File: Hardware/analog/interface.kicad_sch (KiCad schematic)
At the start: 21 parts, among them J301 Conn_02x10_Odd_Even, U301 ADUM131D, U302 ADUM131D, U303 ADUM1250, U304 74LVC1G19

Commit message: More tweaks to load board
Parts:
- added C312: 100nF, Capacitor_SMD:C_0805_2012Metric_Pad1.18x1.45mm_HandSolder, symbol Device:C_Small
- added JP301: Cfg WP, Connector_PinHeader_2.54mm:PinHeader_1x03_P2.54mm_Vertical, symbol Jumper:SolderJumper_3_Bridged12
- added U305: AT24CS32-SSHM, Package_SO:SOIC-8_3.9x4.9mm_P1.27mm, symbol Memory_EEPROM:AT24CS32-SSHM
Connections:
- net +3V3: now also C312.1, JP301.3 (B), U305.8 (VCC)
- net GND: now also C312.2, JP301.1 (A), U305.1 (A0), U305.2 (A1), U305.3 (A2), U305.4 (GND)
- net I2C_SCL: now also U305.6 (SCL)
- net I2C_SDA: now also U305.5 (SDA)
- new net: JP301.2 (C), U305.7 (WP)
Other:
- note added: "IDPROM"
- note added: "I²C address: 0b1010000/0b1011000"

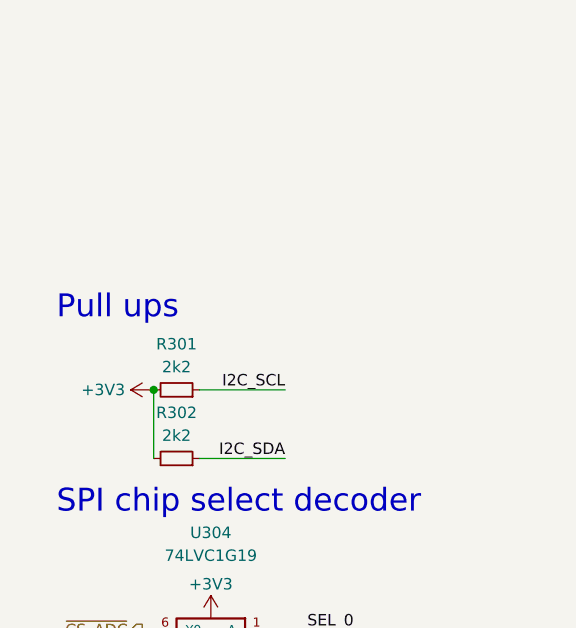
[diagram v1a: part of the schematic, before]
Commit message: Added ADC/DAC section
- Imported the schematic for the analog DAC/ADC section, as well as the
  Vref generator and clock generator for the ADC
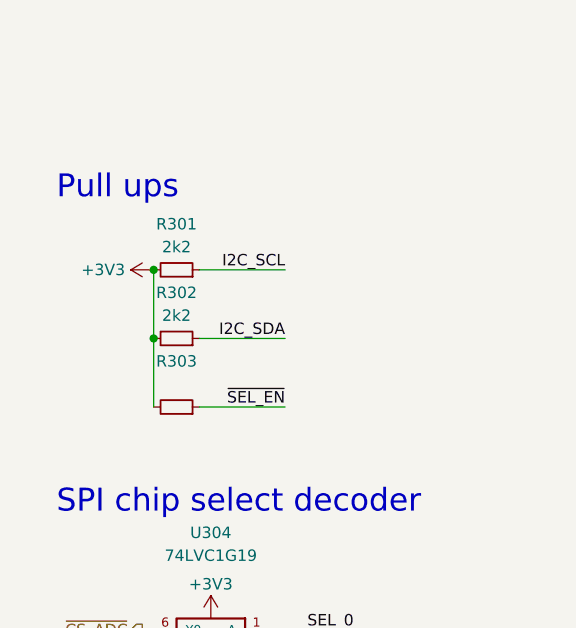
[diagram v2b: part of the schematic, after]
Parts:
- added R303: (no value), symbol Device:R_Small
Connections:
- net +3V3: now also R303.2
- net ~{SEL_EN}: now also R303.1
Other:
- moved on the sheet: R301, R302
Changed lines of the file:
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@@
   (junction (at 175.26 25.4) (diameter 0) (color 0 0 0 0)
   )
+  (junction (at 25.4 151.765) (diameter 0) (color 0 0 0 0)
+  )
   (junction (at 144.78 25.4) (diameter 0) (color 0 0 0 0)
   )
@@
   (junction (at 136.525 30.48) (diameter 0) (color 0 0 0 0)
   )
-  (junction (at 25.4 157.48) (diameter 0) (color 0 0 0 0)
+  (junction (at 25.4 144.145) (diameter 0) (color 0 0 0 0)
   )
   (junction (at 273.05 150.495) (diameter 0) (color 0 0 0 0)
@@
     (stroke (width 0) (type default) (color 0 0 0 0))
   )
-  (wire (pts (xy 40.005 157.48) (xy 30.48 157.48))
+  (wire (pts (xy 40.005 144.145) (xy 30.48 144.145))
     (stroke (width 0) (type default) (color 0 0 0 0))
   )
@@
     (stroke (width 0) (type default) (color 0 0 0 0))
   )
+  (wire (pts (xy 40.005 159.385) (xy 30.48 159.385))
+    (stroke (width 0) (type default) (color 0 0 0 0))
+  )
+  (wire (pts (xy 25.4 151.765) (xy 25.4 159.385))
+    (stroke (width 0) (type default) (color 0 0 0 0))
+  )
   (wire (pts (xy 141.605 80.01) (xy 151.13 80.01))
     (stroke (width 0) (type default) (color 0 0 0 0))
@@
     (stroke (width 0) (type default) (color 0 0 0 0))
   )
-  (wire (pts (xy 40.005 165.1) (xy 30.48 165.1))
+  (wire (pts (xy 40.005 151.765) (xy 30.48 151.765))
     (stroke (width 0) (type default) (color 0 0 0 0))
   )
@@
     (stroke (width 0) (type default) (color 0 0 0 0))
   )
-  (wire (pts (xy 25.4 157.48) (xy 25.4 165.1))
+  (wire (pts (xy 25.4 144.145) (xy 25.4 151.765))
     (stroke (width 0) (type default) (color 0 0 0 0))
   )
@@
     (effects (font (size 1.27 1.27)) (justify left bottom))
   )
-  (text "Pull ups" (at 14.605 149.86 0)
+  (text "Pull ups" (at 14.605 136.525 0)
     (effects (font (size 2.54 2.54)) (justify left bottom))
   )
@@
     (effects (font (size 2.54 2.54)) (justify left bottom))
   )
-  (label "I2C_SDA" (at 40.005 165.1 180)
+  (label "I2C_SDA" (at 40.005 151.765 180)
     (effects (font (size 1.27 1.27)) (justify right bottom))
   )
@@
     (effects (font (size 1.27 1.27)) (justify left bottom))
   )
+  (label "~{SEL_EN}" (at 40.005 159.385 180)
+    (effects (font (size 1.27 1.27)) (justify right bottom))
+  )
   (label "~{IN_SPI_CS}" (at 181.61 77.47 180)
     (effects (font (size 1.27 1.27)) (justify right bottom))
@@
     (effects (font (size 1.27 1.27)) (justify right bottom))
   )
-  (label "I2C_SCL" (at 40.005 157.48 180)
+  (label "I2C_SCL" (at 40.005 144.145 180)
     (effects (font (size 1.27 1.27)) (justify right bottom))
   )
@@
     (pin "1")
   )
-  (symbol (lib_id "Device:R_Small") (at 27.94 165.1 270) (mirror x) (unit 1)
-    (in_bom yes) (on_board yes)
-    (property "Reference" "R302" (id 0) (at 27.94 160.02 90))
-    (property "Value" "2k2" (id 1) (at 27.94 162.56 90))
-    (property "Footprint" "Resistor_SMD:R_0805_2012Metric_Pad1.20x1.40mm_HandSolder" (id 2) (at 27.94 165.1 0)
-      (effects (font (size 1.27 1.27)) hide)
-    )
-    (property "Datasheet" "~" (id 3) (at 27.94 165.1 0)
-      (effects (font (size 1.27 1.27)) hide)
-    )
-    (property "MPN" "RMC1/10-222JTP" (id 4) (at 27.94 165.1 90)
+  (symbol (lib_id "Device:R_Small") (at 27.94 151.765 270) (mirror x) (unit 1)
+    (in_bom yes) (on_board yes)
+    (property "Reference" "R302" (id 0) (at 27.94 146.685 90))
+    (property "Value" "2k2" (id 1) (at 27.94 149.225 90))
+    (property "Footprint" "Resistor_SMD:R_0805_2012Metric_Pad1.20x1.40mm_HandSolder" (id 2) (at 27.94 151.765 0)
+      (effects (font (size 1.27 1.27)) hide)
+    )
+    (property "Datasheet" "~" (id 3) (at 27.94 151.765 0)
+      (effects (font (size 1.27 1.27)) hide)
+    )
+    (property "MPN" "RMC1/10-222JTP" (id 4) (at 27.94 151.765 90)
       (effects (font (size 1.27 1.27)) hide)
     )
@@
     (pin "1")
   )
-  (symbol (lib_id "power:+3V3") (at 25.4 157.48 90) (mirror x) (unit 1)
-    (in_bom yes) (on_board yes) (fields_autoplaced)
-    (property "Reference" "#PWR0331" (id 0) (at 29.21 157.48 0)
-      (effects (font (size 1.27 1.27)) hide)
-    )
-    (property "Value" "+3V3" (id 1) (at 22.225 157.4799 90)
-      (effects (font (size 1.27 1.27)) (justify left))
-    )
-    (property "Footprint" "" (id 2) (at 25.4 157.48 0)
-      (effects (font (size 1.27 1.27)) hide)
-    )
-    (property "Datasheet" "" (id 3) (at 25.4 157.48 0)
+  (symbol (lib_id "power:+3V3") (at 25.4 144.145 90) (mirror x) (unit 1)
+    (in_bom yes) (on_board yes) (fields_autoplaced)
+    (property "Reference" "#PWR0331" (id 0) (at 29.21 144.145 0)
+      (effects (font (size 1.27 1.27)) hide)
+    )
+    (property "Value" "+3V3" (id 1) (at 22.225 144.1449 90)
+      (effects (font (size 1.27 1.27)) (justify left))
+    )
+    (property "Footprint" "" (id 2) (at 25.4 144.145 0)
+      (effects (font (size 1.27 1.27)) hide)
+    )
+    (property "Datasheet" "" (id 3) (at 25.4 144.145 0)
       (effects (font (size 1.27 1.27)) hide)
     )
@@
     )
     (pin "1")
+  )
+  (symbol (lib_id "Device:R_Small") (at 27.94 159.385 270) (mirror x) (unit 1)
+    (in_bom yes) (on_board yes)
+    (property "Reference" "R303" (id 0) (at 27.94 154.305 90))
+    (property "Value" "" (id 1) (at 27.94 156.845 90))
+    (property "Footprint" "" (id 2) (at 27.94 159.385 0)
+      (effects (font (size 1.27 1.27)) hide)
+    )
+    (property "Datasheet" "~" (id 3) (at 27.94 159.385 0)
+      (effects (font (size 1.27 1.27)) hide)
+    )
+    (property "MPN" "RMC1/10-103JTP" (id 4) (at 27.94 159.385 90)
+      (effects (font (size 1.27 1.27)) hide)
+    )
+    (pin "1")
+    (pin "2")
   )
   (symbol (lib_id "power:GND2") (at 190.5 30.48 0) (unit 1)
@@
     (pin "1")
   )
-  (symbol (lib_id "Device:R_Small") (at 27.94 157.48 270) (mirror x) (unit 1)
-    (in_bom yes) (on_board yes)
-    (property "Reference" "R301" (id 0) (at 27.94 152.4 90))
-    (property "Value" "2k2" (id 1) (at 27.94 154.94 90))
-    (property "Footprint" "Resistor_SMD:R_0805_2012Metric_Pad1.20x1.40mm_HandSolder" (id 2) (at 27.94 157.48 0)
-      (effects (font (size 1.27 1.27)) hide)
-    )
-    (property "Datasheet" "~" (id 3) (at 27.94 157.48 0)
-      (effects (font (size 1.27 1.27)) hide)
-    )
-    (property "MPN" "RMC1/10-222JTP" (id 4) (at 27.94 157.48 90)
-      (effects (font (size 1.27 1.27)) hide)
-    )
+  (symbol (lib_id "Device:R_Small") (at 27.94 144.145 270) (mirror x) (unit 1)
+    (in_bom yes) (on_board yes)
+    (property "Reference" "R301" (id 0) (at 27.94 139.065 90))
+    (property "Value" "2k2" (id 1) (at 27.94 141.605 90))
+    (property "Footprint" "Resistor_SMD:R_0805_2012Metric_Pad1.20x1.40mm_HandSolder" (id 2) (at 27.94 144.145 0)
+      (effects (font (size 1.27 1.27)) hide)
+    )
+    (property "Datasheet" "~" (id 3) (at 27.94 144.145 0)
+      (effects (font (size 1.27 1.27)) hide)
+    )
+    (property "MPN" "RMC1/10-222JTP" (id 4) (at 27.94 144.145 90)
+      (effects (font (size 1.27 1.27)) hide)
+    )

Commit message: Add ADC aliasing filters
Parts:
- R303: value (none) -> 10k; footprint (none) -> Resistor_SMD:R_0805_2012Metric_Pad1.20x1.40mm_HandSolder
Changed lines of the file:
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@@
     (in_bom yes) (on_board yes)
     (property "Reference" "R303" (id 0) (at 27.94 154.305 90))
-    (property "Value" "" (id 1) (at 27.94 156.845 90))
-    (property "Footprint" "" (id 2) (at 27.94 159.385 0)
+    (property "Value" "10k" (id 1) (at 27.94 156.845 90))
+    (property "Footprint" "Resistor_SMD:R_0805_2012Metric_Pad1.20x1.40mm_HandSolder" (id 2) (at 27.94 159.385 0)
       (effects (font (size 1.27 1.27)) hide)
     )

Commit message: Start work on analog island
- This is the part with the ADC/DAC/reference which has its own analog
  ground and voltage, generated from +5V
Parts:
- removed R303: 10k, Resistor_SMD:R_0805_2012Metric_Pad1.20x1.40mm_HandSolder, symbol Device:R_Small
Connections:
- net ~{CS_ADC}: now also U304.4 (Y1); no longer U304.6 (Y0)
- net ~{CS_DAC}: now also U304.6 (Y0); no longer U304.4 (Y1)
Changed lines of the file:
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@@
   (junction (at 175.26 25.4) (diameter 0) (color 0 0 0 0)
-  )
-  (junction (at 25.4 151.765) (diameter 0) (color 0 0 0 0)
   )
   (junction (at 144.78 25.4) (diameter 0) (color 0 0 0 0)
@@
     (stroke (width 0) (type default) (color 0 0 0 0))
   )
-  (wire (pts (xy 40.005 159.385) (xy 30.48 159.385))
-    (stroke (width 0) (type default) (color 0 0 0 0))
-  )
-  (wire (pts (xy 25.4 151.765) (xy 25.4 159.385))
-    (stroke (width 0) (type default) (color 0 0 0 0))
-  )
   (wire (pts (xy 141.605 80.01) (xy 151.13 80.01))
     (stroke (width 0) (type default) (color 0 0 0 0))
@@
   (label "IN_SPI_MOSI" (at 228.6 153.035 0)
     (effects (font (size 1.27 1.27)) (justify left bottom))
-  )
-  (label "~{SEL_EN}" (at 40.005 159.385 180)
-    (effects (font (size 1.27 1.27)) (justify right bottom))
   )
   (label "~{IN_SPI_CS}" (at 181.61 77.47 180)
@@
     (effects (font (size 1.27 1.27)) (justify right))
   )
-  (hierarchical_label "~{CS_ADC}" (shape output) (at 24.13 184.15 180)
+  (hierarchical_label "~{CS_ADC}" (shape output) (at 24.13 189.23 180)
     (effects (font (size 1.27 1.27)) (justify right))
   )
@@
     (effects (font (size 1.27 1.27)) (justify right))
   )
-  (hierarchical_label "~{CS_DAC}" (shape output) (at 24.13 189.23 180)
+  (hierarchical_label "~{CS_DAC}" (shape output) (at 24.13 184.15 180)
     (effects (font (size 1.27 1.27)) (justify right))
   )
@@
     (pin "1")
   )
-  (symbol (lib_id "Device:R_Small") (at 27.94 159.385 270) (mirror x) (unit 1)
-    (in_bom yes) (on_board yes)
-    (property "Reference" "R303" (id 0) (at 27.94 154.305 90))
-    (property "Value" "10k" (id 1) (at 27.94 156.845 90))
-    (property "Footprint" "Resistor_SMD:R_0805_2012Metric_Pad1.20x1.40mm_HandSolder" (id 2) (at 27.94 159.385 0)
-      (effects (font (size 1.27 1.27)) hide)
-    )
-    (property "Datasheet" "~" (id 3) (at 27.94 159.385 0)
-      (effects (font (size 1.27 1.27)) hide)
-    )
-    (property "MPN" "RMC1/10-103JTP" (id 4) (at 27.94 159.385 90)
-      (effects (font (size 1.27 1.27)) hide)
-    )
-    (pin "1")
-    (pin "2")
-  )
   (symbol (lib_id "power:GND2") (at 190.5 30.48 0) (unit 1)

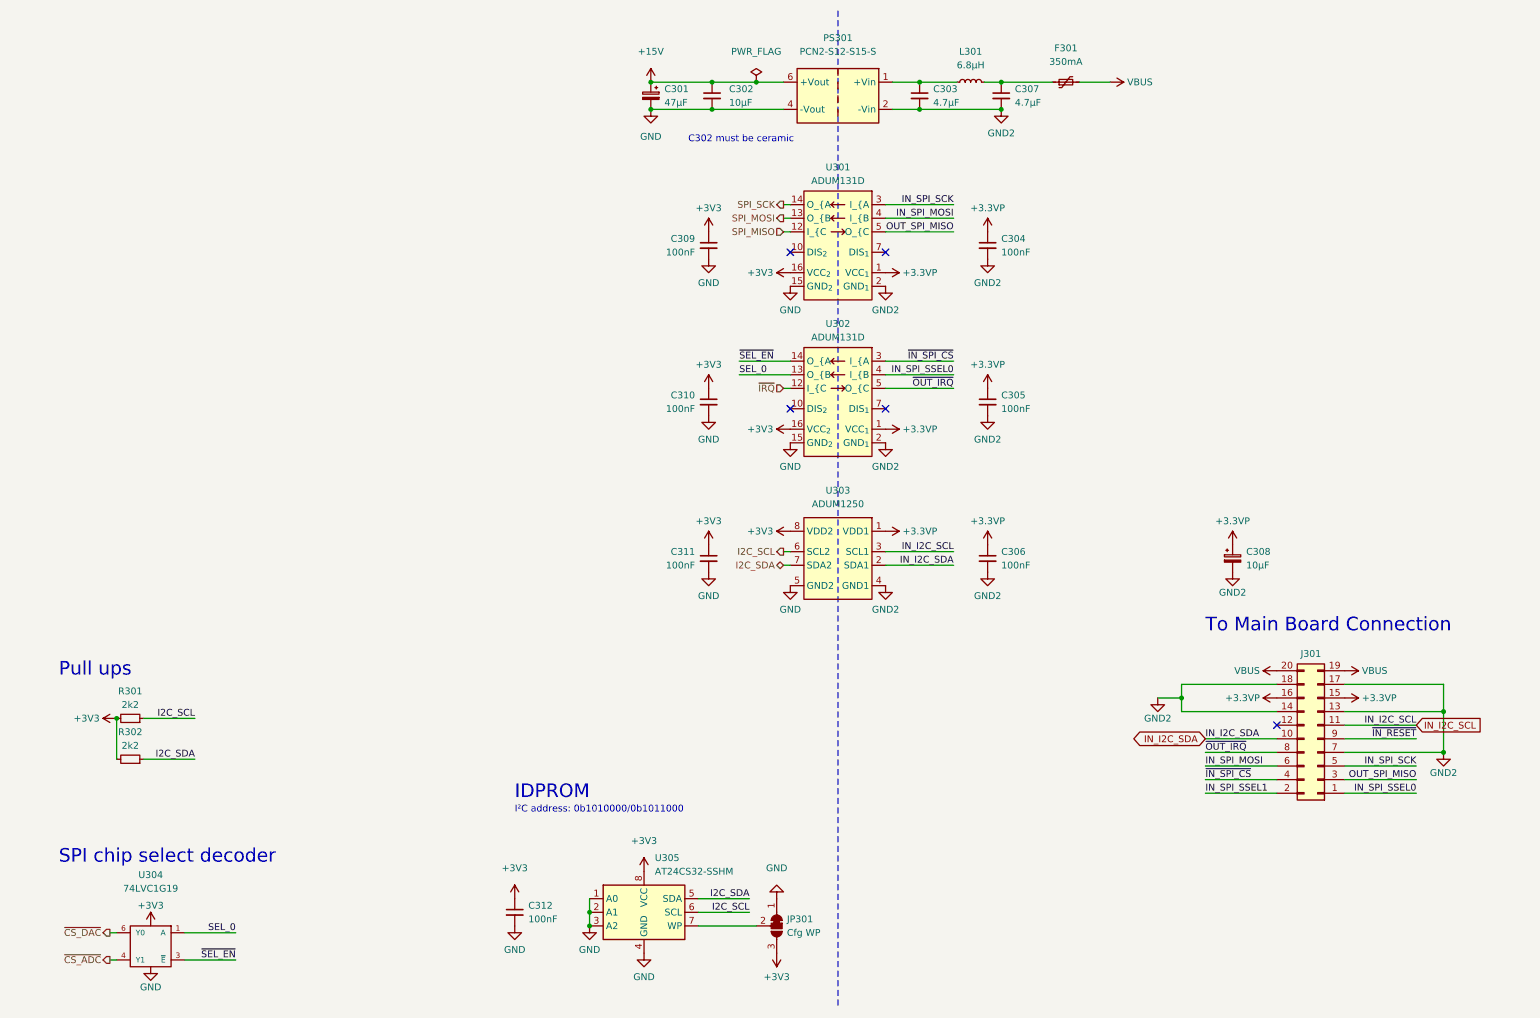
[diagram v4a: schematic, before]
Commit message: Added more decoupling for reference
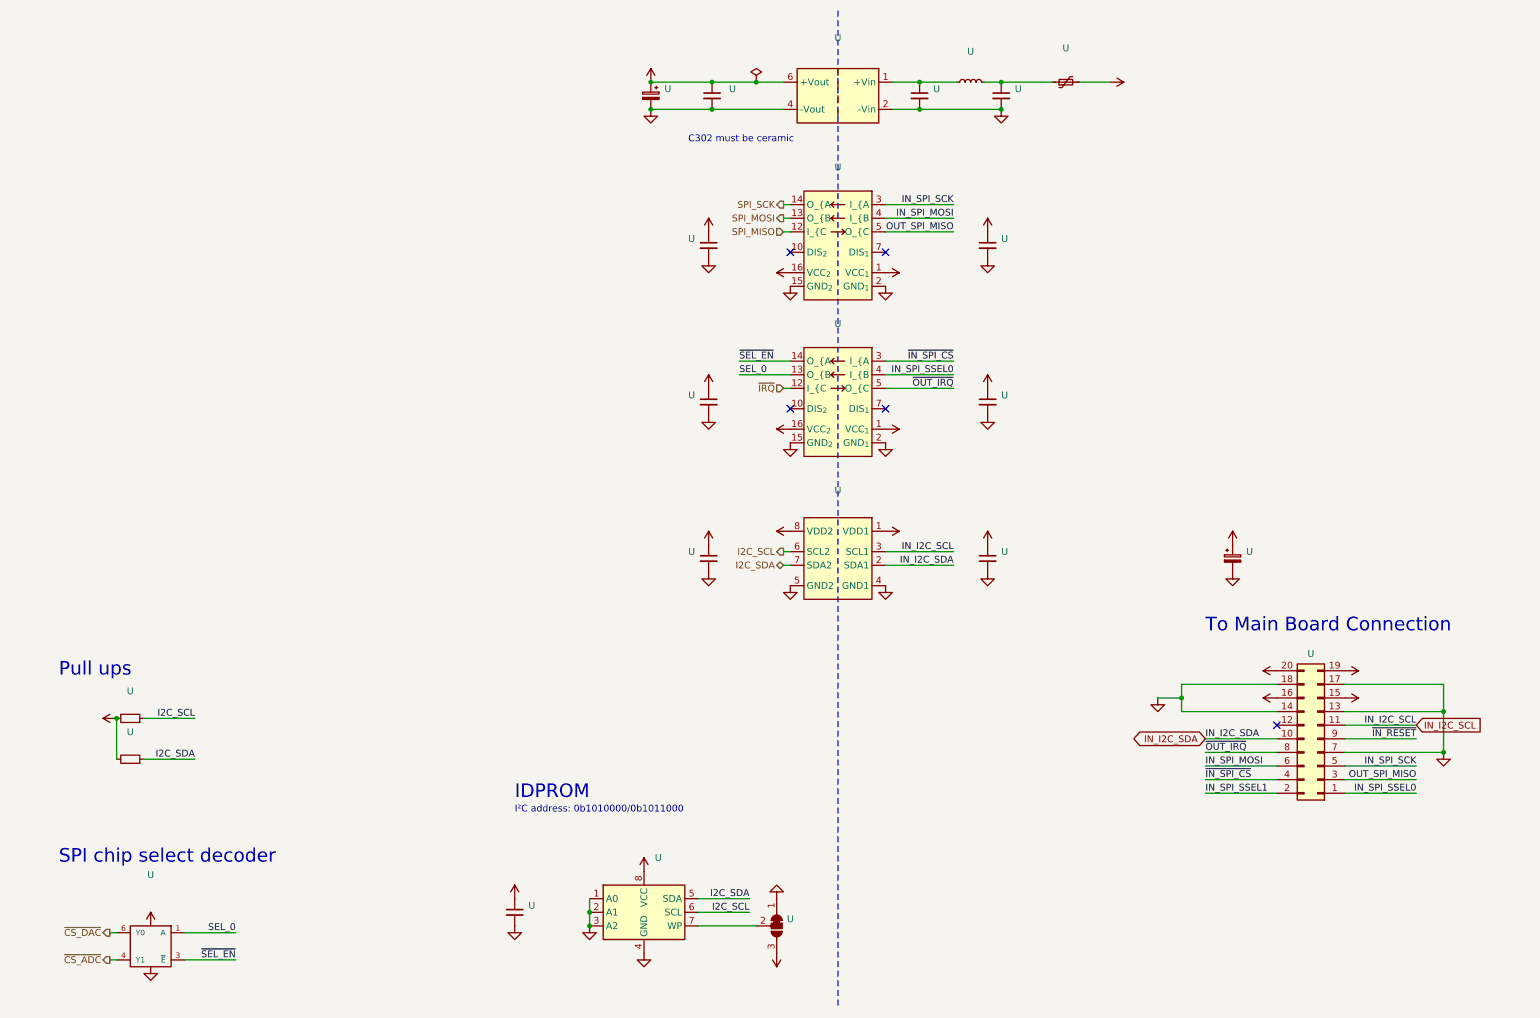
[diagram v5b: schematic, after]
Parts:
- U: renamed from C305; value 100nF -> (none); footprint Capacitor_SMD:C_0805_2012Metric_Pad1.18x1.45mm_HandSolder -> (none)
- U: renamed from R302; value 2k2 -> (none); footprint Resistor_SMD:R_0805_2012Metric_Pad1.20x1.40mm_HandSolder -> (none)
- U: renamed from PS301; value PCN2-S12-S15-S -> (none); footprint programmable-load:CONV_PCN2-S12-S15-S -> (none)
- U: renamed from C311; value 100nF -> (none); footprint Capacitor_SMD:C_0805_2012Metric_Pad1.18x1.45mm_HandSolder -> (none)
- U: renamed from U303; value ADUM1250 -> (none); footprint Package_SO:SOIC-8_3.9x4.9mm_P1.27mm -> (none)
- U: renamed from U305; value AT24CS32-SSHM -> (none); footprint Package_SO:SOIC-8_3.9x4.9mm_P1.27mm -> (none)
- U: renamed from C308; value 10µF -> (none); footprint Capacitor_Tantalum_SMD:CP_EIA-3216-18_Kemet-A_Pad1.58x1.35mm_HandSolder -> (none)
- U: renamed from C304; value 100nF -> (none); footprint Capacitor_SMD:C_0805_2012Metric_Pad1.18x1.45mm_HandSolder -> (none)
- U: renamed from C312; value 100nF -> (none); footprint Capacitor_SMD:C_0805_2012Metric_Pad1.18x1.45mm_HandSolder -> (none)
- U: renamed from C301; value 47µF -> (none); footprint Capacitor_THT:CP_Radial_D6.3mm_P2.50mm -> (none)
- U: renamed from U304; value 74LVC1G19 -> (none); footprint Package_TO_SOT_SMD:TSOT-23-6_HandSoldering -> (none)
- U: renamed from C306; value 100nF -> (none); footprint Capacitor_SMD:C_0805_2012Metric_Pad1.18x1.45mm_HandSolder -> (none)
- U: renamed from C307; value 4.7µF -> (none); footprint Capacitor_SMD:C_0805_2012Metric_Pad1.18x1.45mm_HandSolder -> (none)
- U: renamed from JP301; value Cfg WP -> (none); footprint Connector_PinHeader_2.54mm:PinHeader_1x03_P2.54mm_Vertical -> (none)
- U: renamed from L301; value 6.8µH -> (none); footprint Inductor_SMD:L_Taiyo-Yuden_NR-24xx_HandSoldering -> (none)
- U: renamed from U301; value ADUM131D -> (none); footprint Package_SO:SOIC-16_3.9x9.9mm_P1.27mm -> (none)
- U: renamed from C302; value 10µF -> (none); footprint Capacitor_SMD:C_0805_2012Metric_Pad1.18x1.45mm_HandSolder -> (none)
- U: renamed from J301; value Conn_02x10_Odd_Even -> (none); footprint Connector_IDC:IDC-Header_2x10_P2.54mm_Horizontal -> (none)
- U: renamed from C309; value 100nF -> (none); footprint Capacitor_SMD:C_0805_2012Metric_Pad1.18x1.45mm_HandSolder -> (none)
- U: renamed from R301; value 2k2 -> (none); footprint Resistor_SMD:R_0805_2012Metric_Pad1.20x1.40mm_HandSolder -> (none)
- U: renamed from C303; value 4.7µF -> (none); footprint Capacitor_SMD:C_0805_2012Metric_Pad1.18x1.45mm_HandSolder -> (none)
- U: renamed from U302; value ADUM131D -> (none); footprint Package_SO:SOIC-16_3.9x9.9mm_P1.27mm -> (none)
- U: renamed from C310; value 100nF -> (none); footprint Capacitor_SMD:C_0805_2012Metric_Pad1.18x1.45mm_HandSolder -> (none)
- U: renamed from F301; value 350mA -> (none); footprint Fuse:Fuse_1210_3225Metric_Pad1.42x2.65mm_HandSolder -> (none)
